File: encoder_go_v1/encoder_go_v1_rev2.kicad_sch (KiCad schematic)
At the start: 7 parts, among them J1 BM05B-SRSS-TB_LF__SN_, J2 optional features, U1 MT6701-SOP8

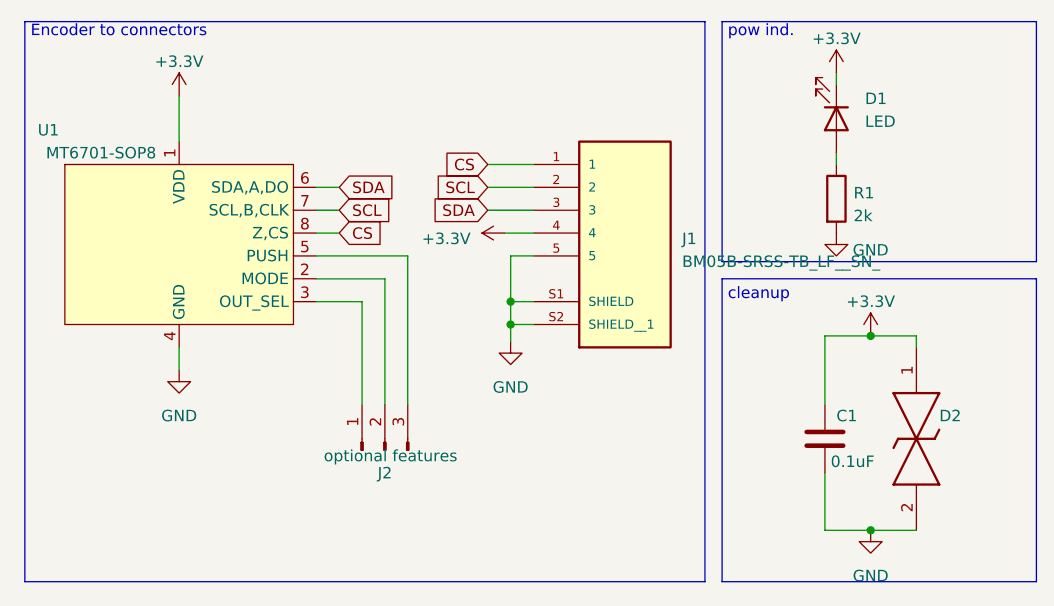
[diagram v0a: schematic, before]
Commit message: copy and modify encodergo for lego
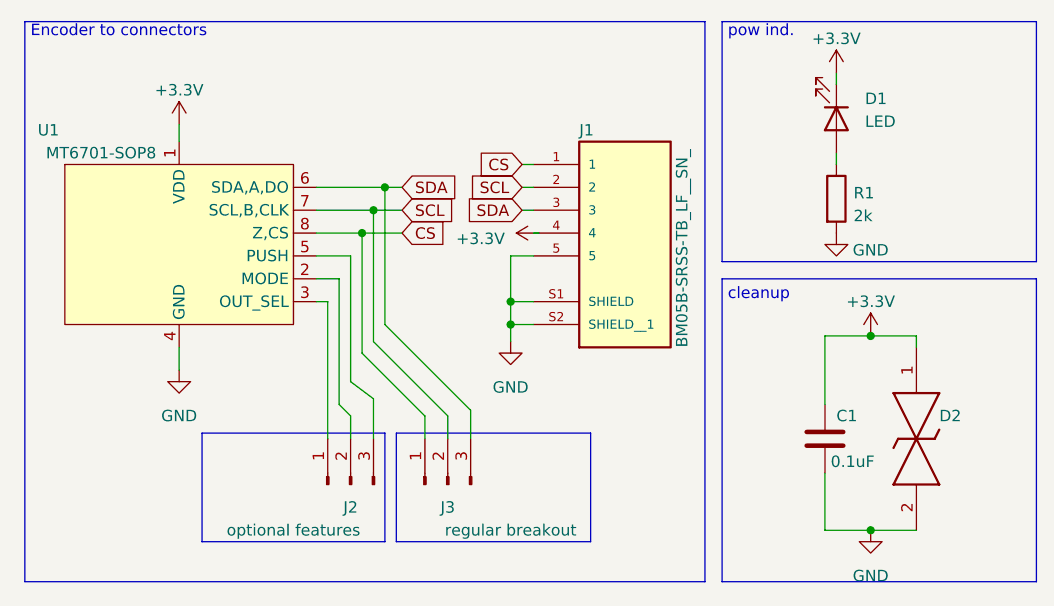
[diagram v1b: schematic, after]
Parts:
- added J3: regular breakout, Connector_PinHeader_2.54mm:PinHeader_1x03_P2.54mm_Horizontal, symbol Connector:Conn_01x03_Pin
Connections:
- net CS: now also J3.1 (Pin_1)
- net SCL: now also J3.2 (Pin_2)
- net SDA: now also J3.3 (Pin_3)
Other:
- moved on the sheet: J2
